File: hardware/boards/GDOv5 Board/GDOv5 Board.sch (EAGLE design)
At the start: 30 parts, among them IC1 DS1820, IC2 3.3V REG, J1 DCJ0202, Q1 BSS84, Q2 BSS138, Q3 BSS138, Q4 IRLML2502

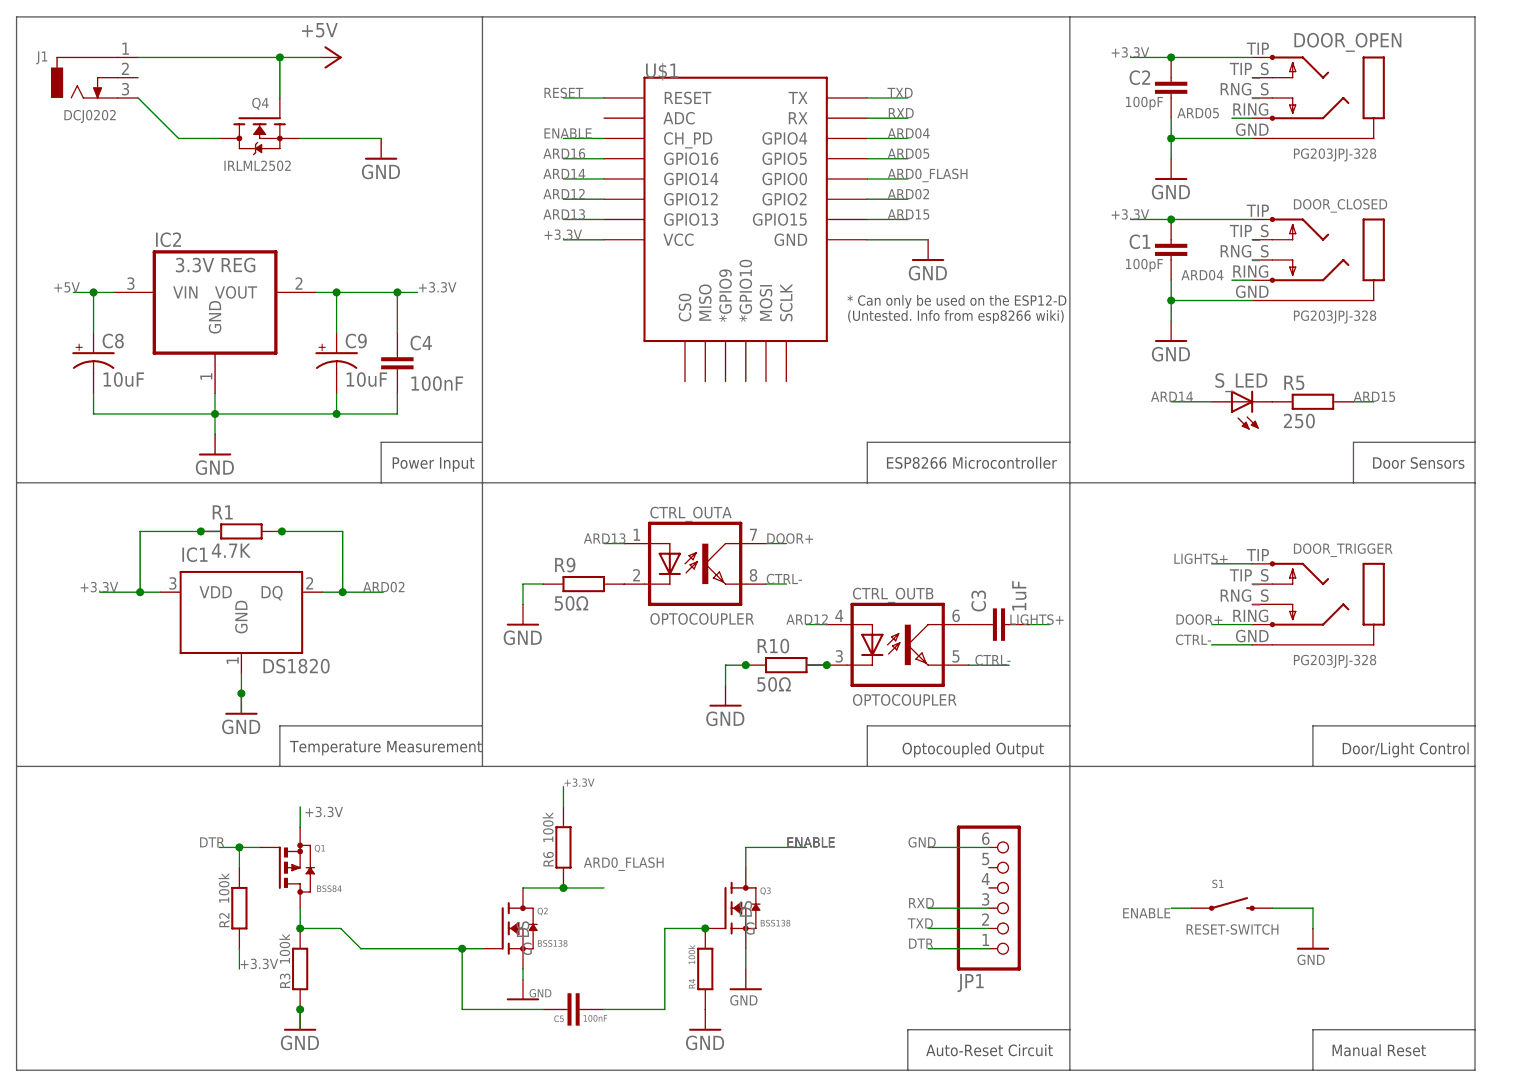
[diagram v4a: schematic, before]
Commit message: Updating board to better match prototype design
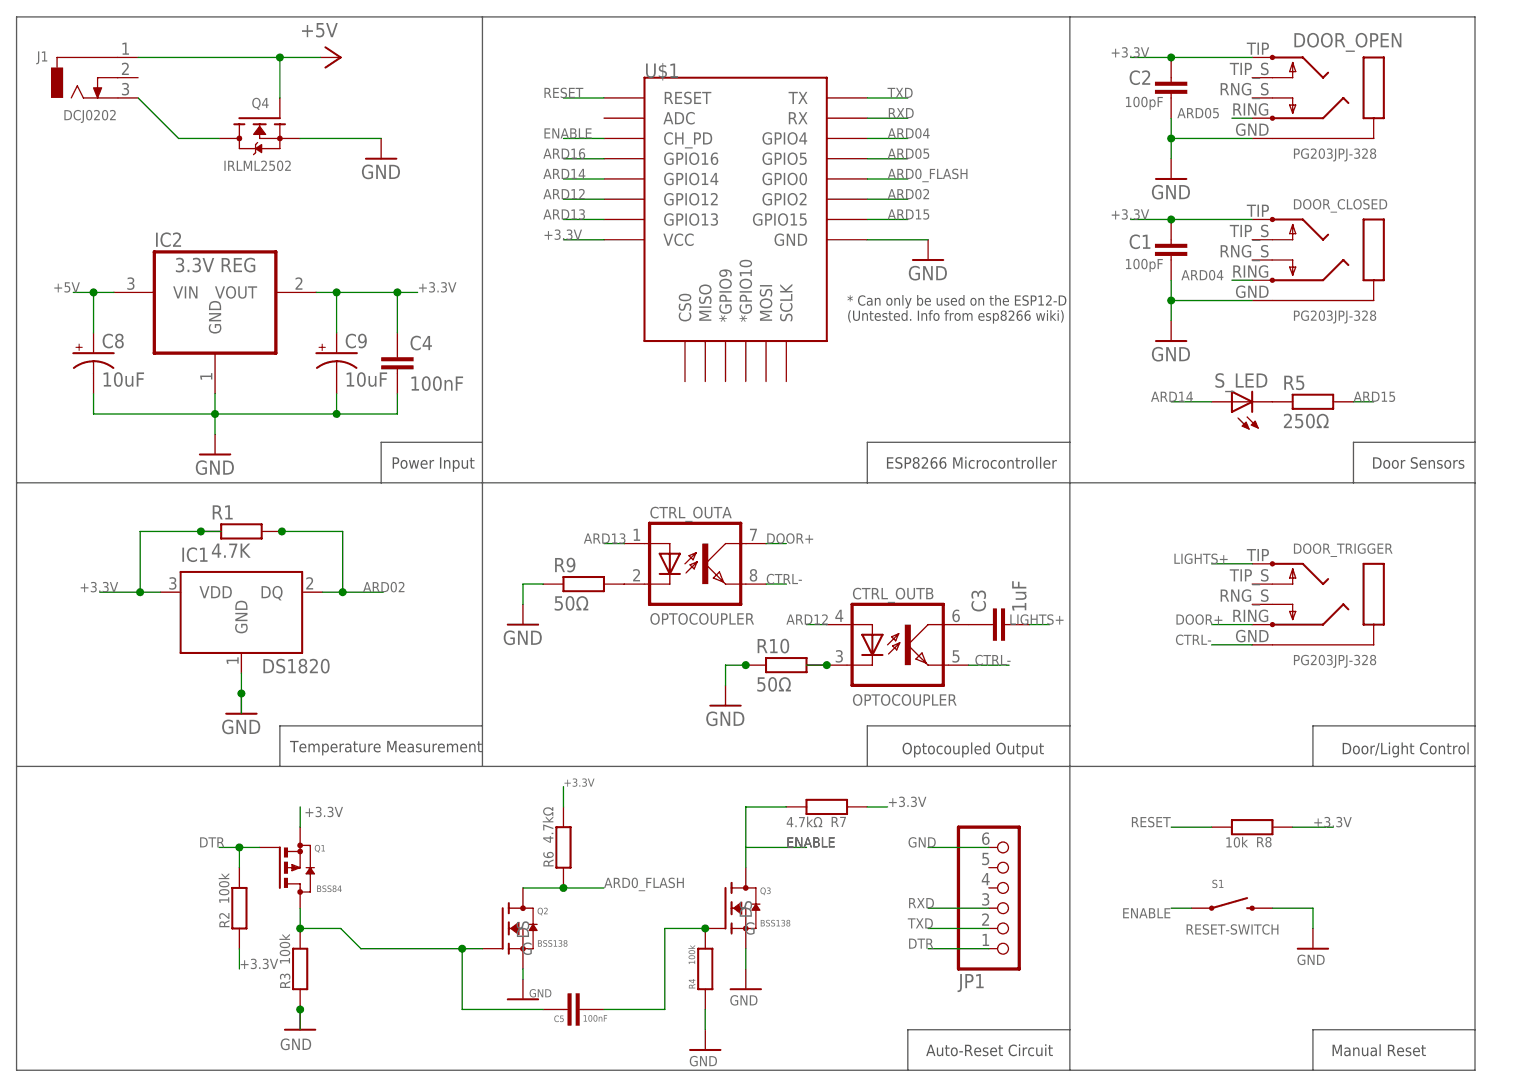
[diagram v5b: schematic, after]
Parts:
- added R7: 4.7kΩ, resistor:R-EU_M3216
- added R8: 10k, resistor:R-EU_M3216
- R5: value 250 -> 250Ω
- R6: value 100k -> 4.7kΩ
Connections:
- net +3.3V: now also R7.1, R8.1
- net ENABLE: now also R7.2
- net RESET: now also R8.2
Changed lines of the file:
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@@
 <part name="JP1" library="adafruit" deviceset="PINHD-1X6" device=""/>
 <part name="S_LED" library="adafruit" deviceset="LED" device="5MM"/>
-<part name="R5" library="resistor" deviceset="R-EU_" device="M3216" value="250"/>
+<part name="R5" library="resistor" deviceset="R-EU_" device="M3216" value="250Ω"/>
 <part name="GND12" library="supply1" deviceset="GND" device=""/>
 <part name="R9" library="resistor" deviceset="R-EU_" device="M3216" value="50Ω"/>
@@
 <part name="C5" library="resistor" deviceset="C-EU" device="C1206" value="100nF"/>
 <part name="R4" library="resistor" deviceset="R-EU_" device="M3216" value="100k"/>
-<part name="GND6" library="supply1" deviceset="GND" device=""/>
 <part name="GND8" library="supply1" deviceset="GND" device=""/>
 <part name="GND9" library="supply1" deviceset="GND" device=""/>
 <part name="GND10" library="supply1" deviceset="GND" device=""/>
-<part name="R6" library="resistor" deviceset="R-EU_" device="M3216" value="100k"/>
+<part name="R6" library="resistor" deviceset="R-EU_" device="M3216" value="4.7kΩ"/>
 <part name="S1" library="SparkFun-Electromechanical" deviceset="SWITCH-MOMENTARY-2" device="-SMD-1101NE" value="RESET-SWITCH"/>
 <part name="GND11" library="supply1" deviceset="GND" device=""/>
@@
 <part name="GND1" library="supply1" deviceset="GND" device=""/>
 <part name="Q4" library="bss138_10" deviceset="BSS138" device="" value="IRLML2502"/>
+<part name="R7" library="resistor" deviceset="R-EU_" device="M3216" value="4.7kΩ"/>
+<part name="R8" library="resistor" deviceset="R-EU_" device="M3216" value="10k"/>
+<part name="GND6" library="supply1" deviceset="GND" device=""/>
 </parts>
 <sheets>
@@
 <attribute name="VALUE" x="54.61" y="-4.572" size="0.8128" layer="96" rot="R90"/>
 </instance>
-<instance part="GND6" gate="1" x="55.88" y="-12.7" smashed="yes">
-<attribute name="VALUE" x="53.34" y="-15.24" size="1.778" layer="96"/>
-</instance>
 <instance part="GND8" gate="1" x="33.02" y="-8.89" smashed="yes">
 <attribute name="VALUE" x="33.782" y="-8.636" size="1.016" layer="96"/>
@@
 </instance>
 <instance part="GND10" gate="1" x="5.08" y="-12.7" smashed="yes">
-<attribute name="VALUE" x="2.54" y="-15.24" size="1.778" layer="96"/>
+<attribute name="VALUE" x="2.54" y="-15.24" size="1.4224" layer="96"/>
 </instance>
 <instance part="R6" gate="G$1" x="38.1" y="10.16" smashed="yes" rot="R90">
@@
 <attribute name="VALUE" x="-4.572" y="96.266" size="1.27" layer="96" rot="MR180"/>
 <attribute name="NAME" x="-1.016" y="104.14" size="1.27" layer="95" rot="MR180"/>
+</instance>
+<instance part="R7" gate="G$1" x="71.12" y="15.24" smashed="yes" rot="R180">
+<attribute name="NAME" x="73.66" y="13.9954" size="1.27" layer="95" rot="R180"/>
+<attribute name="VALUE" x="70.612" y="13.97" size="1.27" layer="96" rot="R180"/>
+</instance>
+<instance part="R8" gate="G$1" x="124.46" y="12.7" smashed="yes" rot="R180">
+<attribute name="NAME" x="127" y="11.4554" size="1.27" layer="95" rot="R180"/>
+<attribute name="VALUE" x="123.952" y="11.43" size="1.27" layer="96" rot="R180"/>
+</instance>
+<instance part="GND6" gate="1" x="55.88" y="-15.24" smashed="yes">
+<attribute name="VALUE" x="53.848" y="-17.272" size="1.27" layer="96"/>
 </instance>
 </instances>
@@
 </segment>
 <segment>
-<pinref part="R4" gate="G$1" pin="1"/>
-<pinref part="GND6" gate="1" pin="GND"/>
-</segment>
-<segment>
 <pinref part="Q2" gate="G$1" pin="S"/>
 <pinref part="GND8" gate="1" pin="GND"/>
@@
 <pinref part="GND1" gate="1" pin="GND"/>
 <wire x1="5.08" y1="99.06" x2="15.24" y2="99.06" width="0.1524" layer="91"/>
+</segment>
+<segment>
+<pinref part="R4" gate="G$1" pin="1"/>
+<wire x1="55.88" y1="-10.16" x2="55.88" y2="-12.7" width="0.1524" layer="91"/>
+<pinref part="GND6" gate="1" pin="GND"/>
 </segment>
 </net>
@@
 <label x="38.1" y="17.78" size="1.016" layer="95"/>
 </segment>
+<segment>
+<pinref part="R7" gate="G$1" pin="1"/>
+<wire x1="76.2" y1="15.24" x2="78.74" y2="15.24" width="0.1524" layer="91"/>
+<label x="78.74" y="15.24" size="1.27" layer="95"/>
+</segment>
+<segment>
+<pinref part="R8" gate="G$1" pin="1"/>
+<wire x1="129.54" y1="12.7" x2="134.62" y2="12.7" width="0.1524" layer="91"/>
+<label x="132.08" y="12.7" size="1.27" layer="95"/>
+</segment>
 </net>
 <net name="ARD05" class="0">
@@
 <pinref part="Q3" gate="G$1" pin="D"/>
 <wire x1="60.96" y1="7.62" x2="60.96" y2="10.16" width="0.1524" layer="91"/>
-<wire x1="60.96" y1="10.16" x2="68.58" y2="10.16" width="0.1524" layer="91"/>
 <label x="66.04" y="10.16" size="1.27" layer="95"/>
 <label x="66.04" y="10.16" size="1.27" layer="95"/>
+<wire x1="60.96" y1="10.16" x2="68.58" y2="10.16" width="0.1524" layer="91"/>
+<wire x1="60.96" y1="10.16" x2="60.96" y2="15.24" width="0.1524" layer="91"/>
+<wire x1="60.96" y1="15.24" x2="66.04" y2="15.24" width="0.1524" layer="91"/>
+<pinref part="R7" gate="G$1" pin="2"/>
 </segment>
 <segment>
@@
 <label x="35.56" y="104.14" size="1.27" layer="95"/>
 </segment>
+<segment>
+<wire x1="114.3" y1="12.7" x2="119.38" y2="12.7" width="0.1524" layer="91"/>
+<pinref part="R8" gate="G$1" pin="2"/>
+<label x="109.22" y="12.7" size="1.27" layer="95"/>
+</segment>
 </net>
 <net name="ARD15" class="0">
@@
 <pinref part="Q2" gate="G$1" pin="D"/>
 <wire x1="33.02" y1="5.08" x2="38.1" y2="5.08" width="0.1524" layer="91"/>
-<label x="40.64" y="7.62" size="1.27" layer="95"/>
+<label x="43.18" y="5.08" size="1.27" layer="95"/>
 <junction x="38.1" y="5.08"/>
 <wire x1="38.1" y1="5.08" x2="43.18" y2="5.08" width="0.1524" layer="91"/>
